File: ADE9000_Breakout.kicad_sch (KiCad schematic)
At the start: 58 parts, among them J1 PWR, J2 Current In, J3 Voltage In, U1 ADE9000, Y1 24.576MHz

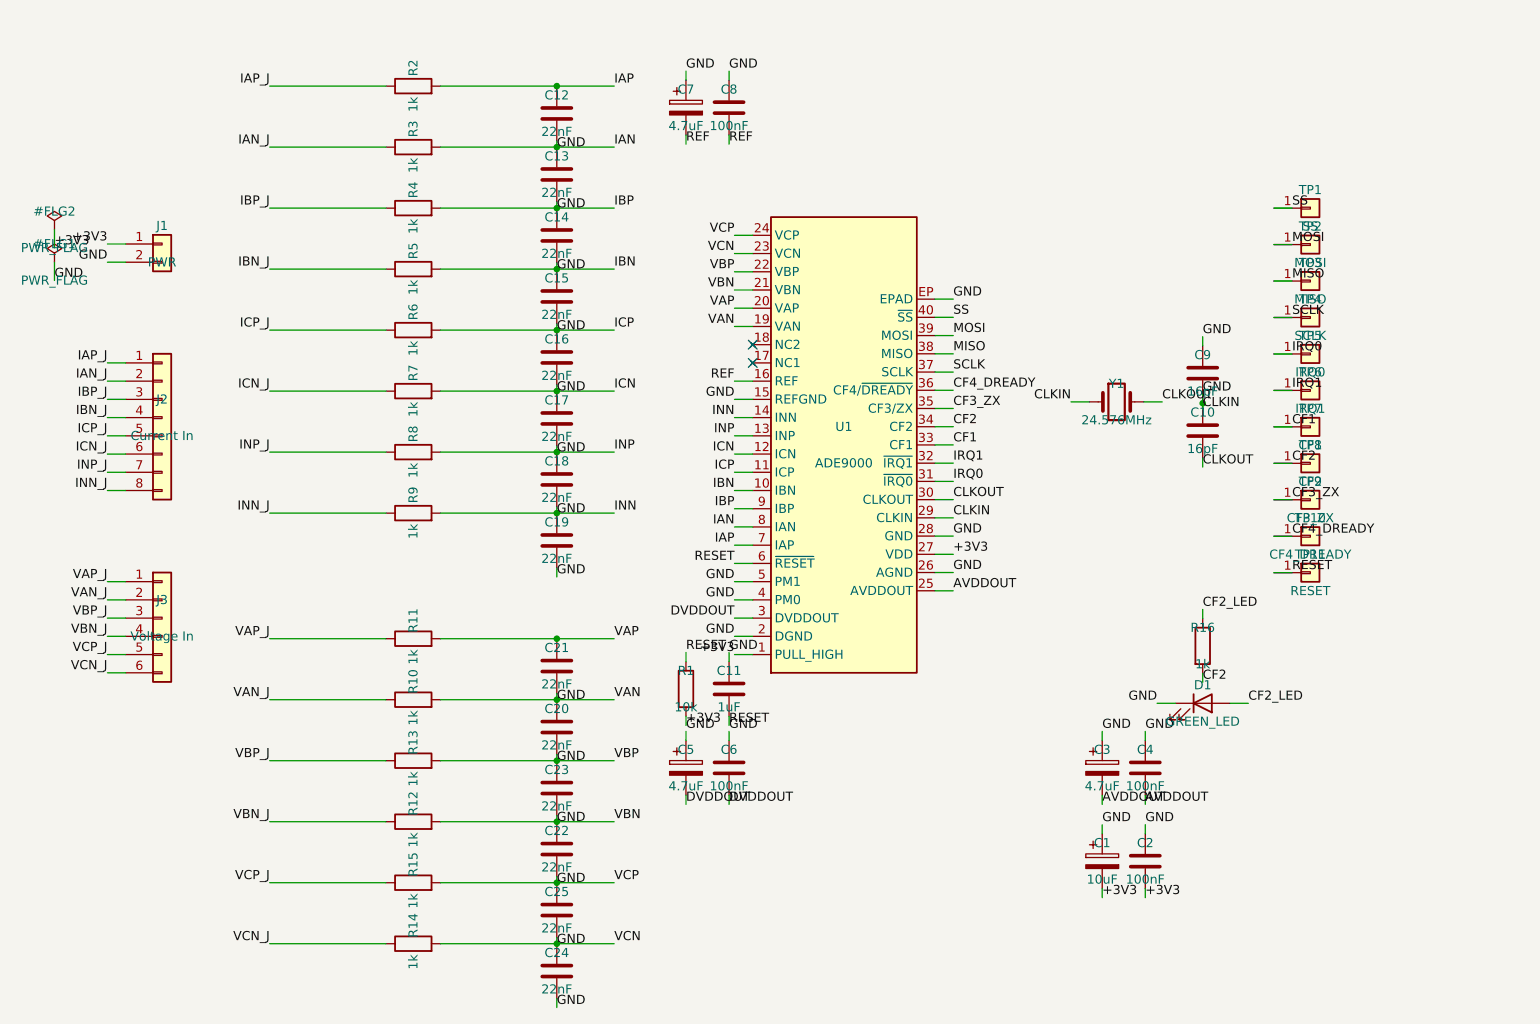
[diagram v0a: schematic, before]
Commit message: Reroute with JST connector for SPI
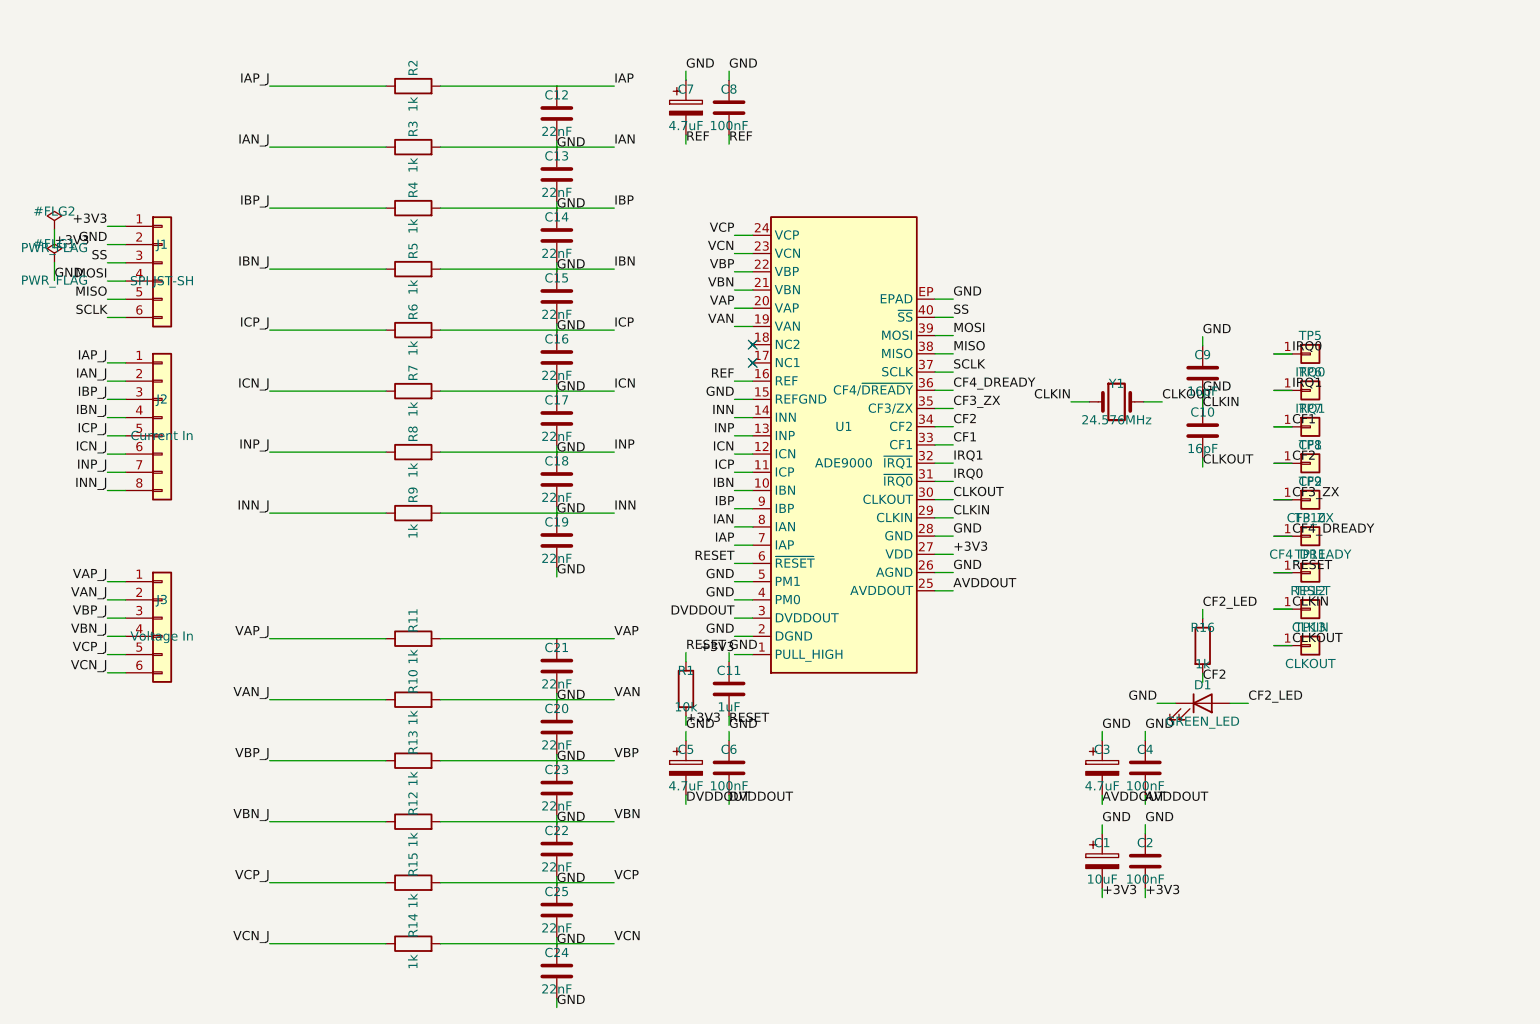
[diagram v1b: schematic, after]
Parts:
- removed TP1: SS, TestPoint:TestPoint_Pad_D1.5mm, symbol Connector_Generic:Conn_01x01
- removed TP2: MOSI, TestPoint:TestPoint_Pad_D1.5mm, symbol Connector_Generic:Conn_01x01
- removed TP3: MISO, TestPoint:TestPoint_Pad_D1.5mm, symbol Connector_Generic:Conn_01x01
- removed TP4: SCLK, TestPoint:TestPoint_Pad_D1.5mm, symbol Connector_Generic:Conn_01x01
- added TP12: CLKIN, TestPoint:TestPoint_Pad_D1.5mm, symbol Connector_Generic:Conn_01x01
- added TP13: CLKOUT, TestPoint:TestPoint_Pad_D1.5mm, symbol Connector_Generic:Conn_01x01
- J1: value PWR -> SPI JST-SH; footprint Connector_PinHeader_2.54mm:PinHeader_1x02_P2.54mm_Vertical -> Connector_JST:JST_SHL_SM06B-SHLS-TF_1x06-1MP_P1.00mm_Horizontal; symbol Connector_Generic:Conn_01x02 -> Connector_Generic:Conn_01x06
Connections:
- net CLKIN: now also TP12.1 (Pin_1); no longer C13.1, C14.1, C15.1, C16.1, C17.1, C18.1, C19.1, C20.1, C22.1, C23.1, C24.1, C25.1, R10.2, R12.2, R13.2, R14.2, R15.2, R3.2, R4.2, R5.2, R6.2, R7.2, R8.2, R9.2, U1.10 (IBN), U1.11 (ICP), U1.12 (ICN), U1.13 (INP), U1.14 (INN), U1.19 (VAN), U1.21 (VBN), U1.22 (VBP), U1.23 (VCN), U1.24 (VCP), U1.8 (IAN), U1.9 (IBP)
- net CLKOUT: now also TP13.1 (Pin_1)
- net MISO: now also J1.5 (Pin_5)
- net MOSI: now also J1.4 (Pin_4)
- net SCLK: now also J1.6 (Pin_6)
- net SS: now also J1.3 (Pin_3)
- new net IAN: C13.1, R3.2, U1.8 (IAN)
- new net IBN: C15.1, R5.2, U1.10 (IBN)
- new net IBP: C14.1, R4.2, U1.9 (IBP)
- new net ICN: C17.1, R7.2, U1.12 (ICN)
- new net ICP: C16.1, R6.2, U1.11 (ICP)
- new net INN: C19.1, R9.2, U1.14 (INN)
- new net INP: C18.1, R8.2, U1.13 (INP)
- new net VAN: C20.1, R10.2, U1.19 (VAN)
- new net VBN: C22.1, R12.2, U1.21 (VBN)
- new net VBP: C23.1, R13.2, U1.22 (VBP)
- new net VCN: C24.1, R14.2, U1.23 (VCN)
- new net VCP: C25.1, R15.2, U1.24 (VCP)

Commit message: Relayout using connectors for analog inputs
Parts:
- removed TP10: CF4_DREADY, TestPoint:TestPoint_Pad_D1.5mm, symbol Connector_Generic:Conn_01x01
- removed TP11: RESET, TestPoint:TestPoint_Pad_D1.5mm, symbol Connector_Generic:Conn_01x01
- removed TP12: CLKIN, TestPoint:TestPoint_Pad_D1.5mm, symbol Connector_Generic:Conn_01x01
- removed TP13: CLKOUT, TestPoint:TestPoint_Pad_D1.5mm, symbol Connector_Generic:Conn_01x01
- removed TP5: IRQ0, TestPoint:TestPoint_Pad_D1.5mm, symbol Connector_Generic:Conn_01x01
- removed TP6: IRQ1, TestPoint:TestPoint_Pad_D1.5mm, symbol Connector_Generic:Conn_01x01
- removed TP7: CF1, TestPoint:TestPoint_Pad_D1.5mm, symbol Connector_Generic:Conn_01x01
- removed TP8: CF2, TestPoint:TestPoint_Pad_D1.5mm, symbol Connector_Generic:Conn_01x01
- removed TP9: CF3_ZX, TestPoint:TestPoint_Pad_D1.5mm, symbol Connector_Generic:Conn_01x01
- added CTA1, CTB1, CTC1, CTN1: CT stereo jack, Connector_Audio:Jack_3.5mm_CUI_SJ-3523-SMT_Horizontal, symbol Connector_Generic:Conn_01x03
- added J4: Voltage terminal, TerminalBlock_4Ucon:TerminalBlock_4Ucon_1x02_P3.50mm_Horizontal, symbol Connector_Generic:Conn_01x02
- J1: value SPI JST-SH -> Digital breadboard; footprint Connector_JST:JST_SHL_SM06B-SHLS-TF_1x06-1MP_P1.00mm_Horizontal -> Connector_PinHeader_2.54mm:PinHeader_1x16_P2.54mm_Vertical; symbol Connector_Generic:Conn_01x06 -> Connector_Generic:Conn_01x16
- J2: value Current In -> Voltage terminal; footprint Connector_PinHeader_2.54mm:PinHeader_1x08_P2.54mm_Vertical -> TerminalBlock_4Ucon:TerminalBlock_4Ucon_1x02_P3.50mm_Horizontal; symbol Connector_Generic:Conn_01x08 -> Connector_Generic:Conn_01x02
- J3: value Voltage In -> Voltage terminal; footprint Connector_PinHeader_2.54mm:PinHeader_1x06_P2.54mm_Vertical -> TerminalBlock_4Ucon:TerminalBlock_4Ucon_1x02_P3.50mm_Horizontal; symbol Connector_Generic:Conn_01x06 -> Connector_Generic:Conn_01x02
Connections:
- net +3V3: no longer J1.1 (Pin_1)
- net CLKIN: no longer J1.2 (Pin_2)
- net IAN_J: no longer J2.2 (Pin_2)
- net IAP_J: no longer J2.1 (Pin_1)
- net IBN_J: no longer J2.4 (Pin_4)
- net IBP_J: no longer J2.3 (Pin_3)
- net ICN_J: no longer J2.6 (Pin_6)
- net ICP_J: no longer J2.5 (Pin_5)
- net INN_J: no longer J2.8 (Pin_8)
- net INP_J: no longer J2.7 (Pin_7)
- net MISO: no longer J1.5 (Pin_5)
- net MOSI: no longer J1.4 (Pin_4)
- net SCLK: no longer J1.6 (Pin_6)
- net SS: no longer J1.3 (Pin_3)
- net VAN_J: now also J2.2 (Pin_2); no longer J3.2 (Pin_2)
- net VAP_J: now also J2.1 (Pin_1); no longer J3.1 (Pin_1)
- net VBN_J: now also J3.2 (Pin_2); no longer J3.4 (Pin_4)
- net VBP_J: now also J3.1 (Pin_1); no longer J3.3 (Pin_3)
- net VCN_J: now also J4.2 (Pin_2); no longer J3.6 (Pin_6)
- net VCP_J: now also J4.1 (Pin_1); no longer J3.5 (Pin_5)
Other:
- moved on the sheet: C12, C13, C14, C15, C16, C17, C18, C19, C20, C21, C22, C23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

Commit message: Rerouted with Groundplanes and new skills
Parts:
- added R17, R18, R19, R20: 2.4R, Resistor_SMD:R_0402_1005Metric, symbol Device:R
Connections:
- net IAN_J: now also R17.2
- net IAP_J: now also R17.1
- net IBN_J: now also R18.2
- net IBP_J: now also R18.1
- net ICN_J: now also R19.2
- net ICP_J: now also R19.1
- net INN_J: now also R20.2
- net INP_J: now also R20.1

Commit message: Use SparkFun locking digital header
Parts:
- J1: footprint Connector_PinHeader_2.54mm:PinHeader_1x16_P2.54mm_Vertical -> SparkFun-Connector:1x16_Locking

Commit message: Add sourced BOM export flow
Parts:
- C1: DigiKey (none) -> https://www.digikey.com/en/products/result?keywords=CL21A10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; MPN (none) -> CL21A106KPFNNNE; Manufacturer (none) -> Samsung Electro-Mechanics; Mouser (none) -> https://www.mouser.com/c/?q=CL21A106KPFNNNE
- C10, C9: DigiKey (none) -> https://www.digikey.com/en/products/result?keywords=GRM1555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; MPN (none) -> GRM1555C1H160JA01D; Manufacturer (none) -> Murata; Mouser (none) -> https://www.mouser.com/c/?q=GRM1555C1H160JA01D
- C11: DigiKey (none) -> https://www.digikey.com/en/products/result?keywords=GRM155R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; MPN (none) -> GRM155R61A105KE15D; Manufacturer (none) -> Murata; Mouser (none) -> https://www.mouser.com/c/?q=GRM155R61A105KE15D
- C12, C13, C14, C15, C16, C17, C18, C19, C20, C21, C22, C23, C24, C25: DigiKey (none) -> https://www.digikey.com/en/products/result?keywords=GRM155R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; MPN (none) -> GRM155R71H223KA12D; Manufacturer (none) -> Murata; Mouser (none) -> https://www.mouser.com/c/?q=GRM155R71H223KA12D
- C2, C4, C6, C8: DigiKey (none) -> https://www.digikey.com/en/products/result?keywords=GRM155R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; MPN (none) -> GRM155R71A104KA01D; Manufacturer (none) -> Murata; Mouser (none) -> https://www.mouser.com/c/?q=GRM155R71A104KA01D
- C3, C5, C7: DigiKey (none) -> https://www.digikey.com/en/products/result?keywords=CL21A47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; MPN (none) -> CL21A475KPFNNNE; Manufacturer (none) -> Samsung Electro-Mechanics; Mouser (none) -> https://www.mouser.com/c/?q=CL21A475KPFNNNE
- CTA1, CTB1, CTC1, CTN1: DigiKey (none) -> https://www.digikey.com/en/products/result?keywords=SJ-3523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; MPN (none) -> SJ-3523-SMT-TR; Manufacturer (none) -> Same Sky; Mouser (none) -> https://www.mouser.com/c/?q=SJ-3523-SMT-TR
- D1: DigiKey (none) -> https://www.digikey.com/en/products/result?keywords=LTST-C1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; MPN (none) -> LTST-C191KGKT; Manufacturer (none) -> Lite-On; Mouser (none) -> https://www.mouser.com/c/?q=LTST-C191KGKT
- J1: DigiKey (none) -> https://www.digikey.com/en/products/result?keywords=PREC016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; MPN (none) -> PREC016SAAN-RC; Manufacturer (none) -> Sullins Connector Solutions; Mouser (none) -> https://www.mouser.com/c/?q=PREC016SAAN-RC
- J2, J3, J4: DigiKey (none) -> https://www.digikey.com/en/products/result?keywords=1984617; MPN (none) -> 1984617; Manufacturer (none) -> Phoenix Contact; Mouser (none) -> https://www.mouser.com/c/?q=1984617
- R1: DigiKey (none) -> https://www.digikey.com/en/products/result?keywords=RC0402F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; MPN (none) -> RC0402FR-0710KL; Manufacturer (none) -> YAGEO; Mouser (none) -> https://www.mouser.com/c/?q=RC0402FR-0710KL
- R10, R11, R12, R13, R14, R15, R16, R2, R3, R4, R5, R6, R7, R8, R9: DigiKey (none) -> https://www.digikey.com/en/products/result?keywords=RC0402F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; MPN (none) -> RC0402FR-071KL; Manufacturer (none) -> YAGEO; Mouser (none) -> https://www.mouser.com/c/?q=RC0402FR-071KL
- R17, R18, R19, R20: DigiKey (none) -> https://www.digikey.com/en/products/result?keywords=RC0402F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; MPN (none) -> RC0402FR-072R4L; Manufacturer (none) -> YAGEO; Mouser (none) -> https://www.mouser.com/c/?q=RC0402FR-072R4L
- U1: DigiKey (none) -> https://www.digikey.com/en/products/result?keywords=ADE9000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; MPN (none) -> ADE9000ACPZ; Manufacturer (none) -> Analog Devices; Mouser (none) -> https://www.mouser.com/c/?q=ADE9000ACPZ
- Y1: DigiKey (none) -> https://www.digikey.com/en/products/result?keywords=ECS-245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; MPN (none) -> ECS-245.7-12-33Q-JES-TR; Manufacturer (none) -> ECS Inc.; Mouser (none) -> https://www.mouser.com/c/?q=ECS-245.7-12-33Q-JES-TR
